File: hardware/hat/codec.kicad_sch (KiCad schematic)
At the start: 62 parts, among them J1 LineOut, J2 Headphone, J3 LineIn, U1 MAX98089ETN_T, Y1 12.288MHz

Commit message: hw:hat
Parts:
- removed C1: 470pF, symbol Device:C_Small
- removed J1: LineOut, symbol Connector_Audio:AudioJack3
- removed J2: Headphone, symbol Connector_Audio:AudioJack4
- removed U1: MAX98089ETN_T, MAX98089ETN_T:QFN40P700X700X80-57N, symbol MAX98089ETN_T:MAX98089ETN_T
- added C10: 470pF, symbol Device:C_Small
- added J2: LineOut, symbol Connector_Audio:AudioJack3
- added J4: Headphone, symbol Connector_Audio:AudioJack4
- added U2: MAX98089ETN_T, MAX98089ETN_T:QFN40P700X700X80-57N, symbol MAX98089ETN_T:MAX98089ETN_T
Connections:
- net +1V8: now also U2.25 (PVDD), U2.50 (AVDD), U2.53 (DVDD)
- net +3V3: now also U2.55 (DVDDS2), U2.6 (DVDDS1)
- net +5V: now also U2.18 (SPKRVDD), U2.19 (SPKLVDD)
- net C1N: now also U2.27 (C1N)
- net C1P: now also U2.26 (C1P)
- net CODEC_BCLKS1: now also U2.8 (BCLKS1)
- net CODEC_LRCLKS1: now also U2.10 (LRCLKS1)
- net CODEC_SCL: now also U2.51 (SCL)
- net CODEC_SDA: now also U2.52 (SDA)
- net CODEC_SDINS1: now also U2.9 (SDINS1)
- net CODEC_SDOUTS1: now also U2.7 (SDOUTS1)
- net CODEC_~{IRQ}: now also U2.56 (~{IRQ})
- net DIGMICCLK: now also U2.41 (MIC1N/DIGMICCLK)
- net DIGMICDATA: now also U2.40 (MIC1P/DIGMICDATA)
- net GND: now also C10.2, J2.S, J4.R2, U2.16 (SPKRGND), U2.21 (SPKLGND), U2.3 (DGND), U2.30 (HPGND), U2.34 (HPSNS), U2.47 (AGND), U2.54 (SDINS2), U2.57 (EP)
- net JackS: now also J4.S, U2.45 (JACKSNS)
- net at D1.3 (TVS2), TP12.1: now also J4.R1, U2.35 (HPR)
- net at D1.1 (TVS1), TP13.1: now also J4.T, U2.33 (HPL)
- net at C2.2, TP2.1: now also J2.T
- net at C111.2, TP21.1: now also U2.38 (INA2/EXTMICN)
- net at C108.2, TP15.1: now also U2.42 (MIC2P)
- net at FB3.1: now also U2.17 (SPKRP)
- net at FB3.2, LS2.1, TP8.1: now also C10.1; no longer C8.1
- net at TP19.1, Y1.3 (OUT): now also U2.5 (MCLK)
- net at C21.1: now also U2.31 (HPVSS)
- net at C110.2, TP20.1: now also U2.39 (INA1/EXTMICP)
- net at C109.2, TP16.1: now also U2.43 (MIC2N)
- net at C22.1: now also U2.32 (HPVDD)
- net at FB1.1: now also U2.20 (SPKLP)
- net at FB1.2, LS1.1, TP4.1: now also C4.1
- net at C19.1: now also U2.49 (REG)
- net at C2.1: now also U2.24 (RECP/LOUTL/RXINP)
- net at FB2.2, LS1.2, TP6.1: now also C8.1; no longer C4.1
- net at C18.1: now also U2.48 (REF)
- net at C3.1: now also U2.23 (RECN/LOUTR/RXINN)
- net at C3.2, TP3.1: now also J2.R
- net at FB4.1: now also U2.15 (SPKRN)
- net at FB2.1: now also U2.22 (SPKLN)
- net at R17.1: now also U2.44 (MICBIAS)

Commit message: hw: assign
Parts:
- C10: renamed from C108; footprint (none) -> Capacitor_SMD:C_0805_2012Metric
- C11: renamed from C109; footprint (none) -> Capacitor_SMD:C_0805_2012Metric
- C12: renamed from C102; footprint (none) -> Capacitor_SMD:C_0805_2012Metric
- C13: renamed from C101; footprint (none) -> Capacitor_SMD:C_0805_2012Metric
- C14: renamed from C23; footprint (none) -> Capacitor_SMD:C_0805_2012Metric
- C15: renamed from C12; footprint (none) -> Capacitor_SMD:C_0805_2012Metric
- C16: renamed from C103; footprint (none) -> Capacitor_SMD:C_0805_2012Metric
- C17: renamed from C107; footprint (none) -> Capacitor_SMD:C_0805_2012Metric
- C18: renamed from C104; footprint (none) -> Capacitor_SMD:C_0805_2012Metric
- C19: renamed from C21; footprint (none) -> Capacitor_SMD:C_0805_2012Metric
- C20, C22: footprint (none) -> Capacitor_SMD:C_0805_2012Metric
- C21: renamed from C105; footprint (none) -> Capacitor_SMD:C_0805_2012Metric
- C23: renamed from C106; footprint (none) -> Capacitor_SMD:C_0805_2012Metric
- C24: renamed from C19; footprint (none) -> Capacitor_SMD:C_0805_2012Metric
- C25: renamed from C18; footprint (none) -> Capacitor_SMD:C_0805_2012Metric
- C26: renamed from C2; footprint (none) -> Capacitor_SMD:C_0805_2012Metric
- C27: renamed from C3; footprint (none) -> Capacitor_SMD:C_0805_2012Metric
- C28: renamed from C4; footprint (none) -> Capacitor_SMD:C_0805_2012Metric
- C29: renamed from C8; footprint (none) -> Capacitor_SMD:C_0805_2012Metric
- C30: renamed from C10; footprint (none) -> Capacitor_SMD:C_0805_2012Metric
- C31: renamed from C11; footprint (none) -> Capacitor_SMD:C_0805_2012Metric
- C4: renamed from C6; footprint (none) -> Capacitor_SMD:C_0805_2012Metric
- C5: renamed from C7; footprint (none) -> Capacitor_SMD:C_0805_2012Metric
- C6: renamed from C9; footprint (none) -> Capacitor_SMD:C_0805_2012Metric
- C7: renamed from C5; footprint (none) -> Capacitor_SMD:C_0805_2012Metric
- C8: renamed from C110; footprint (none) -> Capacitor_SMD:C_0805_2012Metric
- C9: renamed from C111; footprint (none) -> Capacitor_SMD:C_0805_2012Metric
- FB1: renamed from FB6; footprint (none) -> Inductor_SMD:L_0805_2012Metric
- FB2: renamed from FB5; footprint (none) -> Inductor_SMD:L_0805_2012Metric
- FB3: renamed from FB1; footprint (none) -> Inductor_SMD:L_0805_2012Metric
- FB4: renamed from FB2; footprint (none) -> Inductor_SMD:L_0805_2012Metric
- FB5: renamed from FB3; footprint (none) -> Inductor_SMD:L_0805_2012Metric
- FB6: renamed from FB4; footprint (none) -> Inductor_SMD:L_0805_2012Metric
- J3: footprint (none) -> Connector_Audio:Jack_3.5mm_PJ311_Horizontal
- J4: renamed from J2; footprint (none) -> Connector_Audio:Jack_3.5mm_PJ311_Horizontal
- J5: renamed from J4; footprint (none) -> Connector_Audio:Jack_3.5mm_PJ320D_Horizontal
- LS1, LS2: footprint (none) -> TerminalBlock_Phoenix:TerminalBlock_Phoenix_MKDS-1,5-2-5.08_1x02_P5.08mm_Horizontal
- R4: renamed from R16; footprint (none) -> Resistor_SMD:R_0805_2012Metric
- R5: renamed from R17; footprint (none) -> Resistor_SMD:R_0805_2012Metric
- TP1: renamed from TP17; footprint (none) -> TestPoint:TestPoint_Pad_D2.0mm
- TP10: renamed from TP1; footprint (none) -> TestPoint:TestPoint_Pad_D2.0mm
- TP11: renamed from TP2; footprint (none) -> TestPoint:TestPoint_Pad_D2.0mm
- TP12: renamed from TP3; footprint (none) -> TestPoint:TestPoint_Pad_D2.0mm
- TP13: renamed from TP4; footprint (none) -> TestPoint:TestPoint_Pad_D2.0mm
- TP14: renamed from TP6; footprint (none) -> TestPoint:TestPoint_Pad_D2.0mm
- TP15: renamed from TP8; footprint (none) -> TestPoint:TestPoint_Pad_D2.0mm
- TP16: renamed from TP10; footprint (none) -> TestPoint:TestPoint_Pad_D2.0mm
- TP2: renamed from TP20; footprint (none) -> TestPoint:TestPoint_Pad_D2.0mm
- TP3: renamed from TP21; footprint (none) -> TestPoint:TestPoint_Pad_D2.0mm
- TP4: renamed from TP19; footprint (none) -> TestPoint:TestPoint_Pad_D2.0mm
- TP5: renamed from TP15; footprint (none) -> TestPoint:TestPoint_Pad_D2.0mm
- TP6: renamed from TP16; footprint (none) -> TestPoint:TestPoint_Pad_D2.0mm
- TP7: renamed from TP18; footprint (none) -> TestPoint:TestPoint_Pad_D2.0mm
- TP8: renamed from TP12; footprint (none) -> TestPoint:TestPoint_Pad_D2.0mm
- TP9: renamed from TP13; footprint (none) -> TestPoint:TestPoint_Pad_D2.0mm
- U4: renamed from U2; footprint MAX98089ETN_T:QFN40P700X700X80-57N -> footprints:MAX98089ETN_T

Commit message: hw: placement
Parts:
- J3, J4: footprint Connector_Audio:Jack_3.5mm_PJ311_Horizontal -> Connector_Audio:Jack_3.5mm_CUI_SJ-3523-SMT_Horizontal
- J5: footprint Connector_Audio:Jack_3.5mm_PJ320D_Horizontal -> footprints:CUI_SJ-43514-SMT-TR
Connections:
- net at C10.2, TP5.1: now also U4.39 (INA1/EXTMICP); no longer U4.42 (MIC2P)
- net at C9.2, TP3.1: now also U4.43 (MIC2N); no longer U4.38 (INA2/EXTMICN)
- net at C8.2, TP2.1: now also U4.42 (MIC2P); no longer U4.39 (INA1/EXTMICP)
- net at C11.2, TP6.1: now also U4.38 (INA2/EXTMICN); no longer U4.43 (MIC2N)

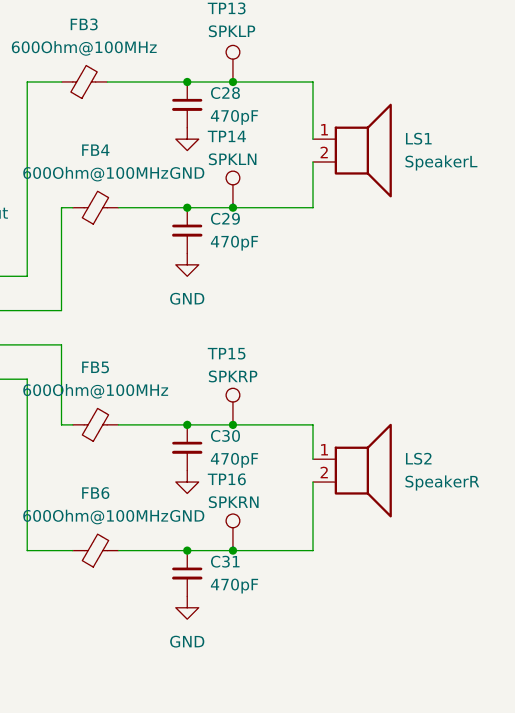
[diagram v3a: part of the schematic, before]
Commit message: all signal except ID chip
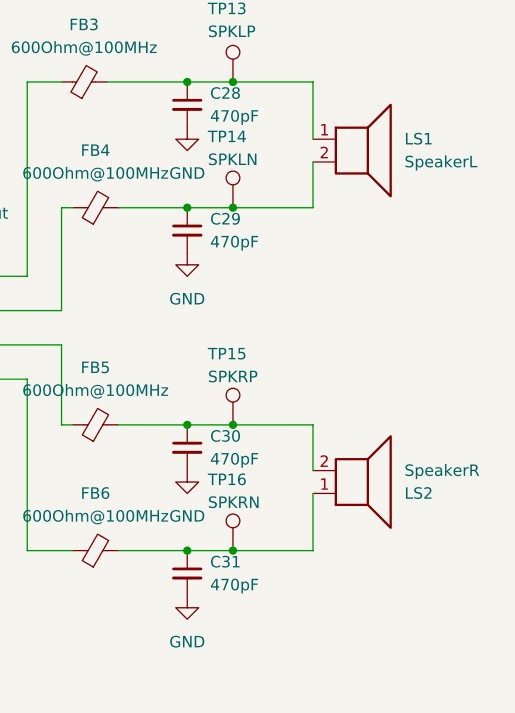
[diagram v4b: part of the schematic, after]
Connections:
- net at C30.1, FB5.2, TP15.1: now also LS2.2; no longer LS2.1
- net at C31.1, FB6.2, TP16.1: now also LS2.1; no longer LS2.2
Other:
- moved on the sheet: LS2
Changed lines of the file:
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@@
 	(wire
 		(pts
-			(xy 261.62 123.19) (xy 261.62 115.57)
+			(xy 261.62 123.19) (xy 261.62 116.84)
 		)
 		(stroke
@@
 	(wire
 		(pts
-			(xy 261.62 85.09) (xy 261.62 80.01)
-		)
-		(stroke
-			(width 0)
-			(type default)
-		)
-	)
-	(wire
-		(pts
 			(xy 161.29 153.67) (xy 161.29 149.86)
 		)
@@
 	(wire
 		(pts
-			(xy 261.62 109.22) (xy 261.62 113.03)
+			(xy 261.62 109.22) (xy 261.62 114.3)
 		)
 		(stroke
@@
 	(wire
 		(pts
+			(xy 261.62 80.01) (xy 261.62 85.09)
+		)
+		(stroke
+			(width 0)
+			(type default)
+		)
+	)
+	(wire
+		(pts
 			(xy 86.36 46.99) (xy 86.36 66.04)
 		)
@@
 	)
 	(symbol
+		(lib_id "Device:Speaker")
+		(at 266.7 77.47 0)
+		(unit 1)
+		(body_style 1)
+		(exclude_from_sim no)
+		(in_bom yes)
+		(on_board yes)
+		(in_pos_files yes)
+		(dnp no)
+		(property "Reference" "LS1"
+			(at 271.78 77.4699 0)
+			(show_name no)
+			(do_not_autoplace no)
+			(effects
+				(font
+					(size 1.27 1.27)
+				)
+				(justify left)
+			)
+		)
+		(property "Value" "SpeakerL"
+			(at 271.78 80.0099 0)
+			(show_name no)
+			(do_not_autoplace no)
+			(effects
+				(font
+					(size 1.27 1.27)
+				)
+				(justify left)
+			)
+		)
+		(property "Footprint" "TerminalBlock_Phoenix:TerminalBlock_Phoenix_MKDS-1,5-2-5.08_1x02_P5.08mm_Horizontal"
+			(at 266.7 82.55 0)
+			(hide yes)
+			(show_name no)
+			(do_not_autoplace no)
+			(effects
+				(font
+					(size 1.27 1.27)
+				)
+			)
+		)
+		(property "Datasheet" ""
+			(at 266.446 78.74 0)
+			(hide yes)
+			(show_name no)
+			(do_not_autoplace no)
+			(effects
+				(font
+					(size 1.27 1.27)
+				)
+			)
+		)
+		(property "Description" "Speaker"
+			(at 266.7 77.47 0)
+			(hide yes)
+			(show_name no)
+			(do_not_autoplace no)
+			(effects
+				(font
+					(size 1.27 1.27)
+				)
+			)
+		)
+		(pin "1"
+		)
+		(pin "2"
+		)
+		(instances
+			(project "hat"
+				(path "/e63e39d7-6ac0-4ffd-8aa3-1841a4541b55/3a835778-dedc-4b02-91df-d91f32dd536d"
+					(reference "LS1")
+					(unit 1)
+				)
+			)
+		)
+	)
+	(symbol
 		(lib_id "Device:C_Small")
 		(at 95.25 118.11 90)
@@
 	)
 	(symbol
-		(lib_id "Device:Speaker")
-		(at 266.7 77.47 0)
-		(unit 1)
-		(body_style 1)
-		(exclude_from_sim no)
-		(in_bom yes)
-		(on_board yes)
-		(in_pos_files yes)
-		(dnp no)
-		(fields_autoplaced yes)
-		(property "Reference" "LS1"
-			(at 271.78 77.4699 0)
-			(show_name no)
-			(do_not_autoplace no)
-			(effects
-				(font
-					(size 1.27 1.27)
-				)
-				(justify left)
-			)
-		)
-		(property "Value" "SpeakerL"
-			(at 271.78 80.0099 0)
-			(show_name no)
-			(do_not_autoplace no)
-			(effects
-				(font
-					(size 1.27 1.27)
-				)
-				(justify left)
-			)
-		)
-		(property "Footprint" "TerminalBlock_Phoenix:TerminalBlock_Phoenix_MKDS-1,5-2-5.08_1x02_P5.08mm_Horizontal"
-			(at 266.7 82.55 0)
-			(hide yes)
-			(show_name no)
-			(do_not_autoplace no)
-			(effects
-				(font
-					(size 1.27 1.27)
-				)
-			)
-		)
-		(property "Datasheet" ""
-			(at 266.446 78.74 0)
-			(hide yes)
-			(show_name no)
-			(do_not_autoplace no)
-			(effects
-				(font
-					(size 1.27 1.27)
-				)
-			)
-		)
-		(property "Description" "Speaker"
-			(at 266.7 77.47 0)
-			(hide yes)
-			(show_name no)
-			(do_not_autoplace no)
-			(effects
-				(font
-					(size 1.27 1.27)
-				)
-			)
-		)
-		(pin "1"
-		)
-		(pin "2"
-		)
-		(instances
-			(project "hat"
-				(path "/e63e39d7-6ac0-4ffd-8aa3-1841a4541b55/3a835778-dedc-4b02-91df-d91f32dd536d"
-					(reference "LS1")
-					(unit 1)
-				)
-			)
-		)
-	)
-	(symbol
 		(lib_id "power:GND")
 		(at 41.91 92.71 0)
@@
 	(symbol
 		(lib_id "Device:Speaker")
-		(at 266.7 113.03 0)
+		(at 266.7 116.84 0)
+		(mirror x)
 		(unit 1)
 		(body_style 1)
@@
 		(in_pos_files yes)
 		(dnp no)
-		(fields_autoplaced yes)
 		(property "Reference" "LS2"
-			(at 271.78 113.0299 0)
+			(at 271.78 116.8401 0)
 			(show_name no)
 			(do_not_autoplace no)
@@
 		)
 		(property "Value" "SpeakerR"
-			(at 271.78 115.5699 0)
+			(at 271.78 114.3001 0)
 			(show_name no)
 			(do_not_autoplace no)
@@
 		)
 		(property "Footprint" "TerminalBlock_Phoenix:TerminalBlock_Phoenix_MKDS-1,5-2-5.08_1x02_P5.08mm_Horizontal"
-			(at 266.7 118.11 0)
+			(at 266.7 111.76 0)
 			(hide yes)
 			(show_name no)
@@
 		)
 		(property "Datasheet" ""
-			(at 266.446 114.3 0)
+			(at 266.446 115.57 0)
 			(hide yes)
 			(show_name no)
@@
 		)
 		(property "Description" "Speaker"
-			(at 266.7 113.03 0)
+			(at 266.7 116.84 0)
 			(hide yes)
 			(show_name no)

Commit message: wip
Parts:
- TP1, TP10, TP11, TP12, TP13, TP14, TP15, TP16, TP2, TP3, TP4, TP5, TP6, TP7, TP8, TP9: now not fitted
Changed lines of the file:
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@@
 		(on_board yes)
 		(in_pos_files yes)
-		(dnp no)
+		(dnp yes)
 		(property "Reference" "TP6"
 			(at 96.774 126.746 0)
@@
 		(on_board yes)
 		(in_pos_files yes)
-		(dnp no)
+		(dnp yes)
 		(property "Reference" "TP1"
 			(at 86.36 86.868 0)
@@
 		(on_board yes)
 		(in_pos_files yes)
-		(dnp no)
+		(dnp yes)
 		(property "Reference" "TP2"
 			(at 100.33 110.744 0)
@@
 		(on_board yes)
 		(in_pos_files yes)
-		(dnp no)
+		(dnp yes)
 		(property "Reference" "TP15"
 			(at 249.936 101.346 0)
@@
 		(on_board yes)
 		(in_pos_files yes)
-		(dnp no)
+		(dnp yes)
 		(property "Reference" "TP5"
 			(at 96.774 122.174 0)
@@
 		(on_board yes)
 		(in_pos_files yes)
-		(dnp no)
+		(dnp yes)
 		(property "Reference" "TP13"
 			(at 249.936 62.992 0)
@@
 		(on_board yes)
 		(in_pos_files yes)
-		(dnp no)
+		(dnp yes)
 		(fields_autoplaced yes)
 		(property "Reference" "TP10"
@@
 		(on_board yes)
 		(in_pos_files yes)
-		(dnp no)
+		(dnp yes)
 		(property "Reference" "TP14"
 			(at 249.936 77.216 0)
@@
 		(on_board yes)
 		(in_pos_files yes)
-		(dnp no)
+		(dnp yes)
 		(property "Reference" "TP12"
 			(at 200.66 92.2021 0)
@@
 		(on_board yes)
 		(in_pos_files yes)
-		(dnp no)
+		(dnp yes)
 		(property "Reference" "TP16"
 			(at 249.936 115.316 0)
@@
 		(on_board yes)
 		(in_pos_files yes)
-		(dnp no)
+		(dnp yes)
 		(property "Reference" "TP4"
 			(at 101.6 61.468 0)
@@
 		(on_board yes)
 		(in_pos_files yes)
-		(dnp no)
+		(dnp yes)
 		(fields_autoplaced yes)
 		(property "Reference" "TP11"
@@
 		(on_board yes)
 		(in_pos_files yes)
-		(dnp no)
+		(dnp yes)
 		(property "Reference" "TP9"
 			(at 187.96 119.888 0)
@@
 		(on_board yes)
 		(in_pos_files yes)
-		(dnp no)
+		(dnp yes)
 		(property "Reference" "TP8"
 			(at 187.198 101.092 0)
@@
 		(on_board yes)
 		(in_pos_files yes)
-		(dnp no)
+		(dnp yes)
 		(property "Reference" "TP7"
 			(at 181.356 125.984 0)
@@
 		(on_board yes)
 		(in_pos_files yes)
-		(dnp no)
+		(dnp yes)
 		(property "Reference" "TP3"
 			(at 100.33 115.824 0)

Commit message: restore backup from June 6 1:34 AM
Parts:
- C10, C11, C13, C15, C16, C18, C19, C20, C21, C22, C24, C8, C9: LCSC (none) -> C28323
- C12, C23: value 0.1uF -> 100nF; LCSC (none) -> C49678
- C14, C17, C26, C27: LCSC (none) -> C15850
- C25: LCSC (none) -> C377773
- C28, C29, C30, C31: LCSC (none) -> C1743
- C4, C5, C6: value 0.1uF X7R -> 100nF; LCSC (none) -> C49678
- C7: LCSC (none) -> C14857
- D1: LCSC (none) -> C495220
- FB1, FB2, FB3, FB4, FB5, FB6: LCSC (none) -> C341663
- J3, J4: now not fitted
- J5: LCSC (none) -> C4992301
- LS1, LS2: LCSC (none) -> C474881
- MK1, MK2: LCSC (none) -> C2879853
- R4: LCSC (none) -> C17414
- R5: LCSC (none) -> C17520
- U4: LCSC (none) -> C2651816
- Y1: LCSC (none) -> C20617595
